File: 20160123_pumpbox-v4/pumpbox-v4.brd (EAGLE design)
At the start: 61 x 38.1 mm, 7 parts

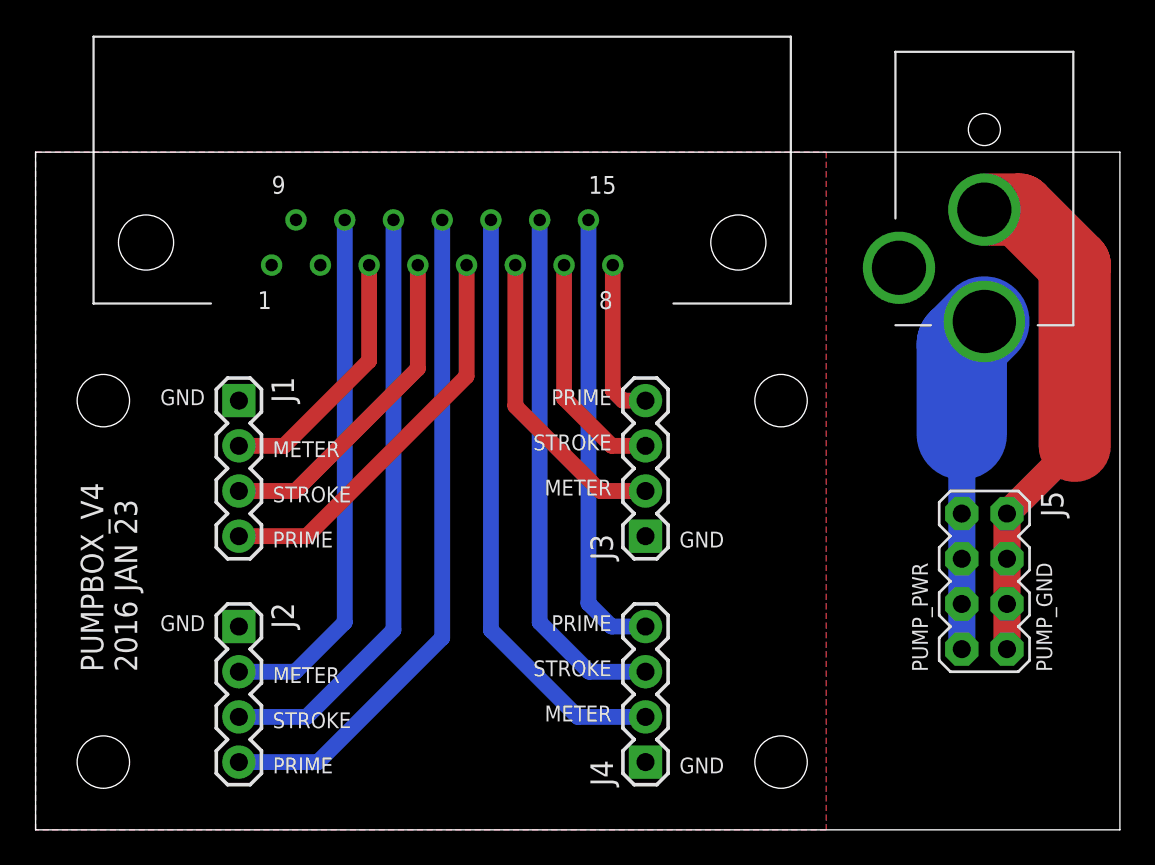
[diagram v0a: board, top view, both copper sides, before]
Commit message: Retract the DB15 header
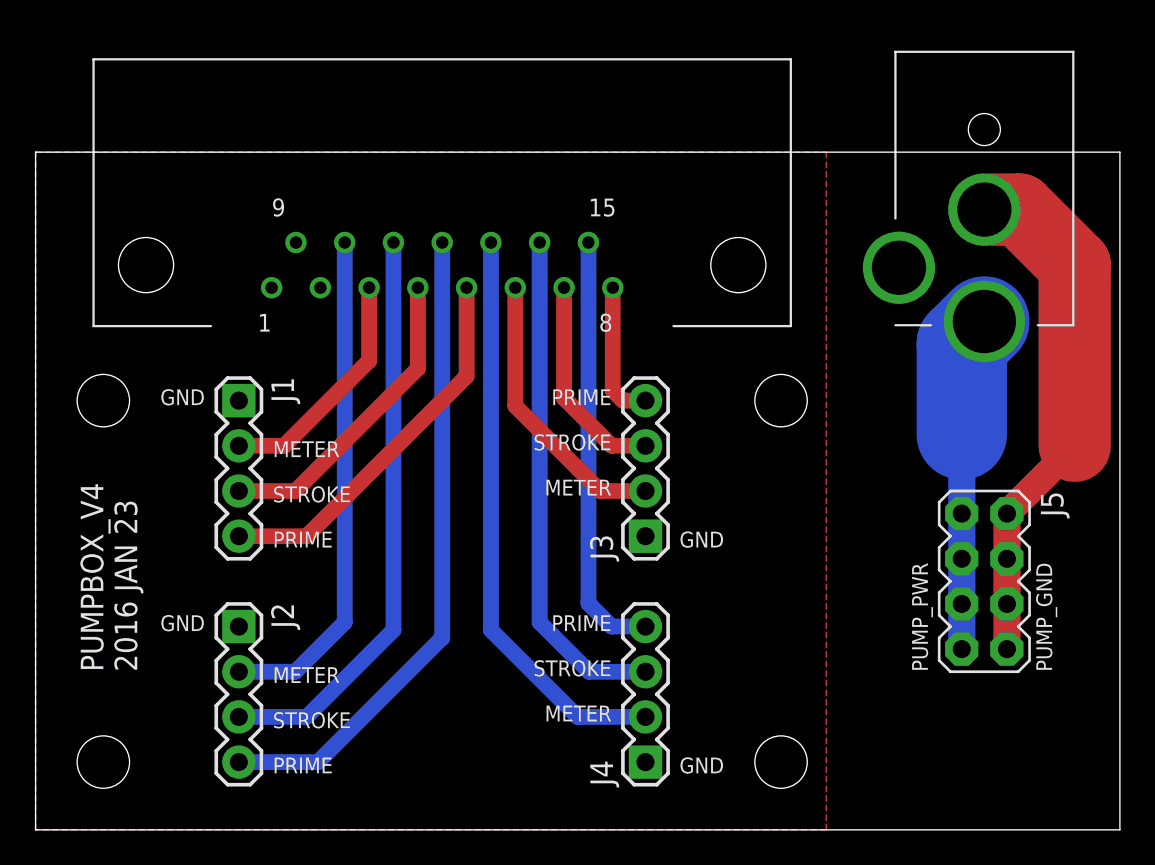
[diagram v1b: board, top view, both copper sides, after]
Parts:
- moved U$1 1.27 mm to (22.9, 31.8)
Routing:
- net 1PRIME: track 22.8 -> 21.5 mm
- net 3PRIME: track 9.13 -> 7.86 mm
- net 3STROKE: track 13.2 -> 11.9 mm
- net 3METER: track 17.2 -> 15.9 mm
- net 1STROKE: track 18.7 -> 17.5 mm
- net 1METER: track 14.7 -> 13.4 mm
- net 4STROKE: track 29.7 -> 28.5 mm
- net 4PRIME: track 25.3 -> 24.0 mm
- net 4METER: track 33.8 -> 32.5 mm
- net 2STROKE: track 33.8 -> 32.5 mm
- net 2PRIME: track 37.8 -> 36.5 mm
- net 2METER: track 29.7 -> 28.5 mm
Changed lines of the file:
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@@
 </autorouter>
 <elements>
-<element name="U$1" library="kimth" package="DB15" value="DB15" x="22.86" y="33.02" rot="R180"/>
+<element name="U$1" library="kimth" package="DB15" value="DB15" x="22.86" y="31.75" rot="R180"/>
 <element name="J1" library="SparkFun-Connectors" package="1X04" value="" x="11.43" y="24.13" rot="R270">
 <attribute name="PROD_ID" value="CONN-09696" x="11.43" y="24.13" size="1.778" layer="27" rot="R270" display="off"/>
@@
 <contactref element="U$1" pad="P$3"/>
 <contactref element="J1" pad="2"/>
-<wire x1="18.75" y1="31.75" x2="18.75" y2="26.37" width="0.889" layer="1"/>
+<wire x1="18.75" y1="30.48" x2="18.75" y2="26.37" width="0.889" layer="1"/>
 <wire x1="18.75" y1="26.37" x2="13.97" y2="21.59" width="0.889" layer="1"/>
 <wire x1="13.97" y1="21.59" x2="11.43" y2="21.59" width="0.889" layer="1"/>
@@
 <contactref element="U$1" pad="P$4"/>
 <contactref element="J1" pad="3"/>
-<wire x1="21.49" y1="31.75" x2="21.49" y2="25.935" width="0.889" layer="1"/>
+<wire x1="21.49" y1="30.48" x2="21.49" y2="25.935" width="0.889" layer="1"/>
 <wire x1="21.49" y1="25.935" x2="14.605" y2="19.05" width="0.889" layer="1"/>
 <wire x1="14.605" y1="19.05" x2="11.43" y2="19.05" width="0.889" layer="1"/>
@@
 <contactref element="U$1" pad="P$5"/>
 <contactref element="J1" pad="4"/>
-<wire x1="24.23" y1="31.75" x2="24.23" y2="25.5" width="0.889" layer="1"/>
+<wire x1="24.23" y1="30.48" x2="24.23" y2="25.5" width="0.889" layer="1"/>
 <wire x1="24.23" y1="25.5" x2="15.24" y2="16.51" width="0.889" layer="1"/>
 <wire x1="15.24" y1="16.51" x2="11.43" y2="16.51" width="0.889" layer="1"/>
@@
 <contactref element="U$1" pad="P$6"/>
 <contactref element="J3" pad="2"/>
-<wire x1="26.97" y1="31.75" x2="26.97" y2="23.83" width="0.889" layer="1"/>
+<wire x1="26.97" y1="30.48" x2="26.97" y2="23.83" width="0.889" layer="1"/>
 <wire x1="26.97" y1="23.83" x2="31.75" y2="19.05" width="0.889" layer="1"/>
 <wire x1="31.75" y1="19.05" x2="34.29" y2="19.05" width="0.889" layer="1"/>
@@
 <contactref element="U$1" pad="P$7"/>
 <contactref element="J3" pad="3"/>
-<wire x1="29.71" y1="31.75" x2="29.71" y2="24.265" width="0.889" layer="1"/>
+<wire x1="29.71" y1="30.48" x2="29.71" y2="24.265" width="0.889" layer="1"/>
 <wire x1="29.71" y1="24.265" x2="32.385" y2="21.59" width="0.889" layer="1"/>
 <wire x1="32.385" y1="21.59" x2="34.29" y2="21.59" width="0.889" layer="1"/>
@@
 <contactref element="U$1" pad="P$8"/>
 <contactref element="J3" pad="4"/>
-<wire x1="32.45" y1="31.75" x2="32.45" y2="24.7" width="0.889" layer="1"/>
+<wire x1="32.45" y1="30.48" x2="32.45" y2="24.7" width="0.889" layer="1"/>
 <wire x1="32.45" y1="24.7" x2="33.02" y2="24.13" width="0.889" layer="1"/>
 <wire x1="33.02" y1="24.13" x2="34.29" y2="24.13" width="0.889" layer="1"/>
@@
 <contactref element="U$1" pad="P$10"/>
 <contactref element="J2" pad="2"/>
-<wire x1="17.38" y1="34.29" x2="17.38" y2="11.665" width="0.889" layer="16"/>
+<wire x1="17.38" y1="33.02" x2="17.38" y2="11.665" width="0.889" layer="16"/>
 <wire x1="17.38" y1="11.665" x2="14.605" y2="8.89" width="0.889" layer="16"/>
 <wire x1="14.605" y1="8.89" x2="11.43" y2="8.89" width="0.889" layer="16"/>
@@
 <contactref element="J2" pad="3"/>
 <contactref element="U$1" pad="P$11"/>
-<wire x1="20.12" y1="34.29" x2="20.12" y2="11.23" width="0.889" layer="16"/>
+<wire x1="20.12" y1="33.02" x2="20.12" y2="11.23" width="0.889" layer="16"/>
 <wire x1="20.12" y1="11.23" x2="15.24" y2="6.35" width="0.889" layer="16"/>
 <wire x1="15.24" y1="6.35" x2="11.43" y2="6.35" width="0.889" layer="16"/>
@@
 <contactref element="J2" pad="4"/>
 <contactref element="U$1" pad="P$12"/>
-<wire x1="22.86" y1="34.29" x2="22.86" y2="10.795" width="0.889" layer="16"/>
+<wire x1="22.86" y1="33.02" x2="22.86" y2="10.795" width="0.889" layer="16"/>
 <wire x1="22.86" y1="10.795" x2="15.875" y2="3.81" width="0.889" layer="16"/>
 <wire x1="15.875" y1="3.81" x2="11.43" y2="3.81" width="0.889" layer="16"/>
@@
 <contactref element="U$1" pad="P$13"/>
 <contactref element="J4" pad="2"/>
-<wire x1="25.6" y1="34.29" x2="25.6" y2="11.23" width="0.889" layer="16"/>
+<wire x1="25.6" y1="33.02" x2="25.6" y2="11.23" width="0.889" layer="16"/>
 <wire x1="25.6" y1="11.23" x2="30.48" y2="6.35" width="0.889" layer="16"/>
 <wire x1="30.48" y1="6.35" x2="34.29" y2="6.35" width="0.889" layer="16"/>
@@
 <contactref element="U$1" pad="P$14"/>
 <contactref element="J4" pad="3"/>
-<wire x1="28.34" y1="34.29" x2="28.34" y2="11.665" width="0.889" layer="16"/>
+<wire x1="28.34" y1="33.02" x2="28.34" y2="11.665" width="0.889" layer="16"/>
 <wire x1="28.34" y1="11.665" x2="31.115" y2="8.89" width="0.889" layer="16"/>
 <wire x1="31.115" y1="8.89" x2="34.29" y2="8.89" width="0.889" layer="16"/>
@@
 <contactref element="U$1" pad="P$15"/>
 <contactref element="J4" pad="4"/>
-<wire x1="31.08" y1="34.29" x2="31.08" y2="12.735" width="0.889" layer="16"/>
+<wire x1="31.08" y1="33.02" x2="31.08" y2="12.735" width="0.889" layer="16"/>
 <wire x1="31.08" y1="12.735" x2="32.385" y2="11.43" width="0.889" layer="16"/>
 <wire x1="32.385" y1="11.43" x2="34.29" y2="11.43" width="0.889" layer="16"/>
